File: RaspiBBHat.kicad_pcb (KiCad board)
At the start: 2 copper layers, 58.4 x 66 mm, 9 parts, among them J1 Conn_01x03, J2 Conn_01x16, J3 Conn_01x03, J4 Conn_01x16, J5 Raspberry_Pi_2_3

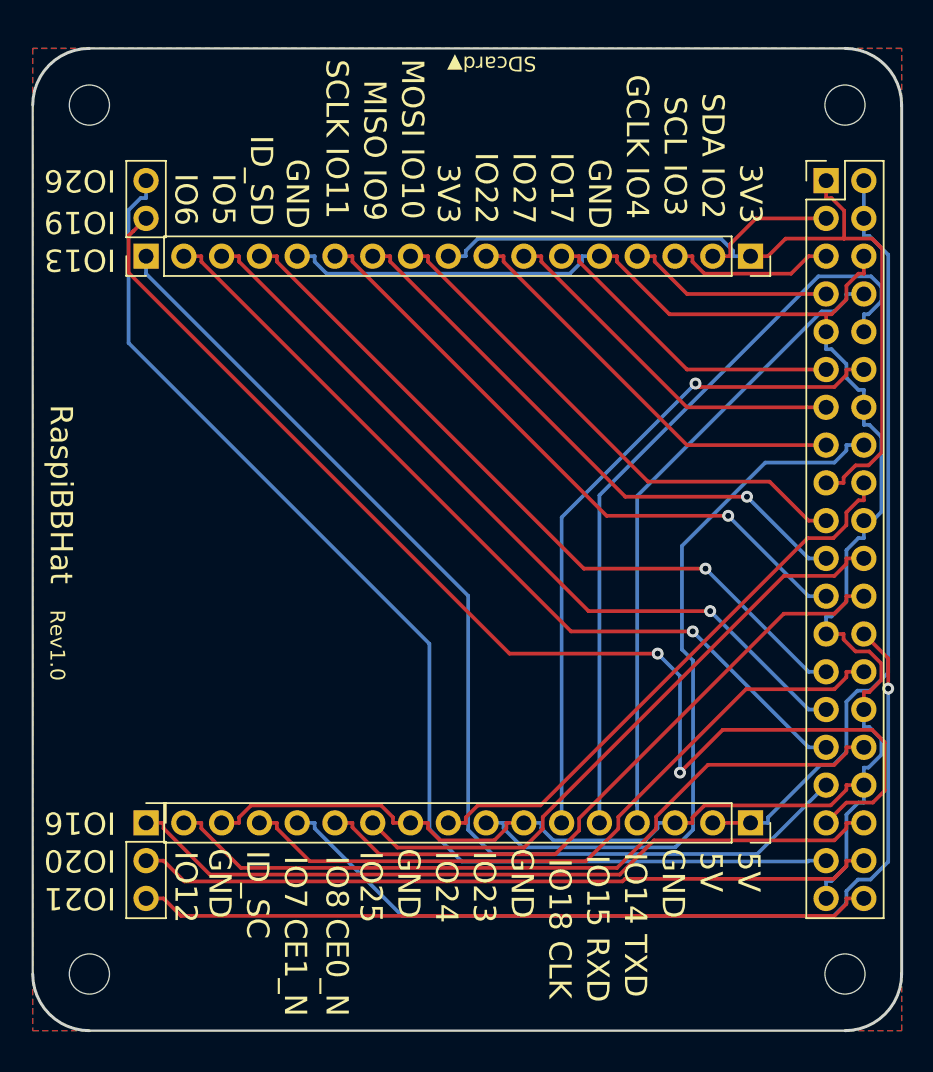
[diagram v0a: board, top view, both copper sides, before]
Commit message: Update hole and label position for rev 1.1
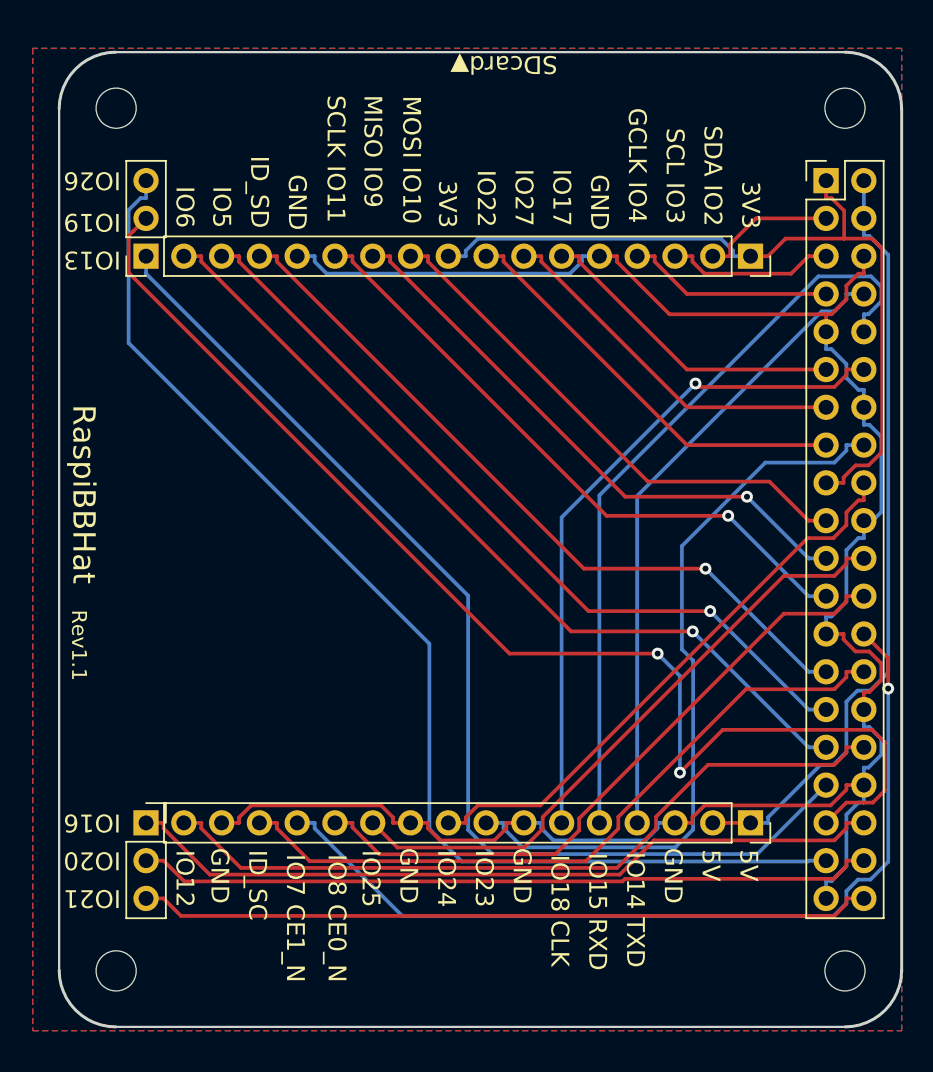
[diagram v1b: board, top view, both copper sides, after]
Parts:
- moved REF1 1.81 mm to (76.1, 71.3)
- moved REF4 1.81 mm to (76.1, 129.3)
- moved REF2 0.21 mm to (125.1, 71.3)
- moved REF3 0.21 mm to (125.1, 129.3)
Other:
- board size 58.4 x 66 mm -> 56.6 x 65.5 mm
- board text added: "Rev1.1"
- board text removed: "Rev1.0"
